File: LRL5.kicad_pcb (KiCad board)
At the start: 2 copper layers, 140 x 50 mm, 31 parts, among them J1 POWER, J2 On/Off, J5 OUT, J6 MODE, Q1 BC549, U1 BA033CC0T, U2 NHD-C0220BIZ

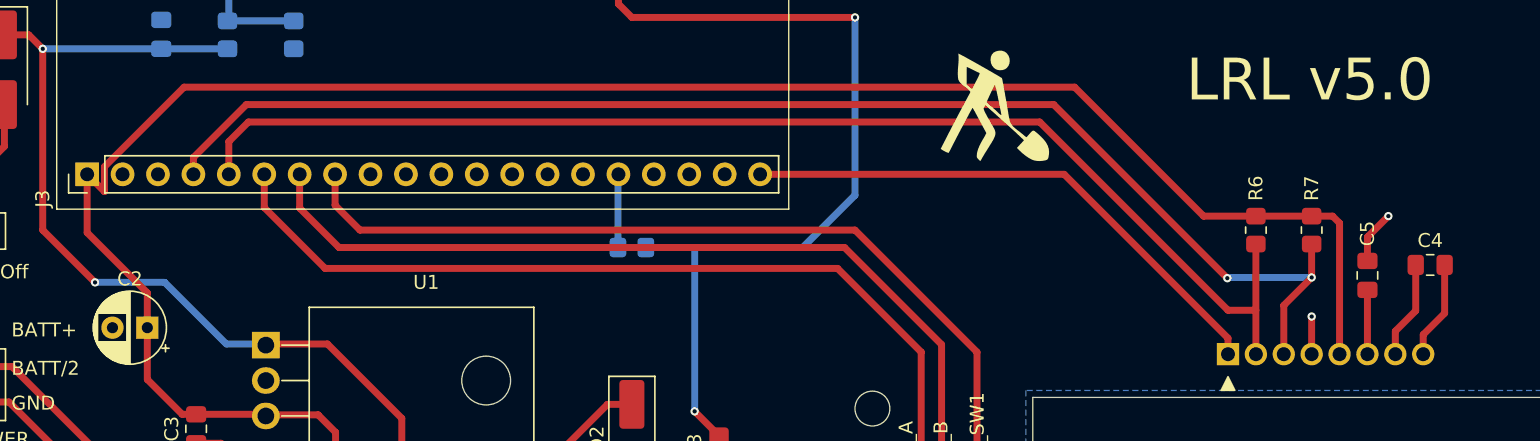
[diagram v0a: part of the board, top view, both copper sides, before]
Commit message: Fix some wires
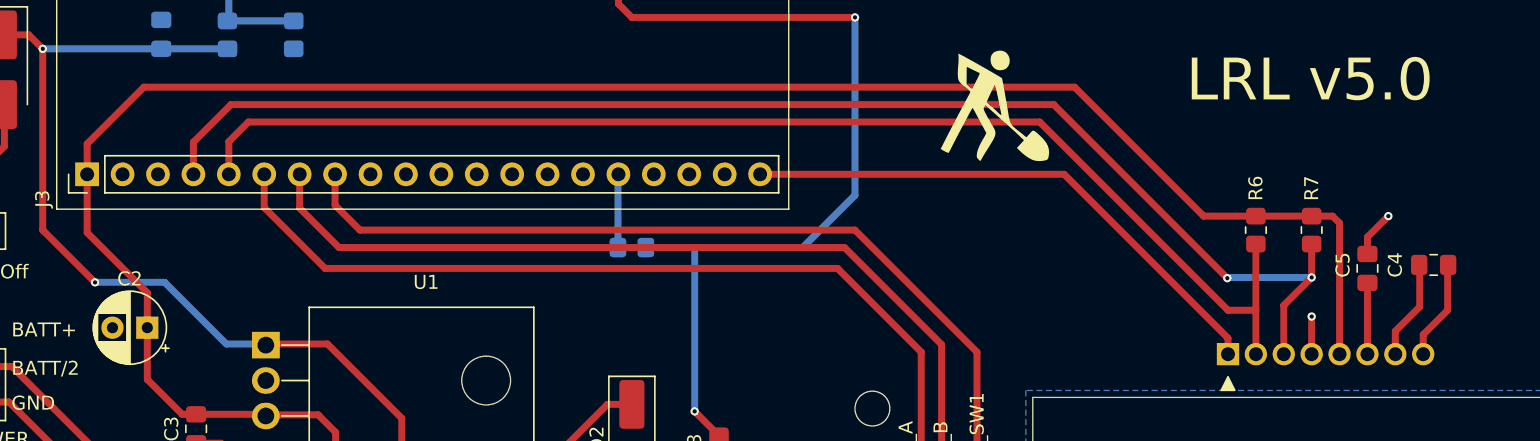
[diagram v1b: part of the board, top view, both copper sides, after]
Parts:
- moved C5 0.50 mm to (229.0, 57.8)
- moved C4 0.25 mm to (233.8, 57.5)
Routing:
- net +3.3V: track 146.8 -> 146.0 mm
- net I2C1_SDA: track 96.9 -> 97.5 mm
- net Net-(U2-VOUT): track 4.61 -> 5.11 mm
- net GND: track 43.4 -> 42.9 mm
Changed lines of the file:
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@@
 	(footprint "Capacitor_SMD:C_0805_2012Metric_Pad1.18x1.45mm_HandSolder"
 		(layer "F.Cu")
-		(at 233.5 57.5)
+		(at 233.75 57.5)
 		(descr "Capacitor SMD 0805 (2012 Metric), square (rectangular) end terminal, IPC_7351 nominal with elongated pad for handsoldering. (Body size source: IPC-SM-782 page 76, https://www.pcb-3d.com/wordpress/wp-content/uploads/ipc-sm-782a_amendment_1_and_2.pdf, https://docs.google.com/spreadsheets/d/1BsfQQcO9C6DZCsRaXUlFlo91Tg2WpOkGARC1WS5S8t0/edit?usp=sharing), generated with kicad-footprint-generator")
 		(tags "capacitor handsolder")
 		(property "Reference" "C4"
-			(at 0 -1.75 0)
+			(at -2.75 0 90)
 			(layer "F.SilkS")
 			(effects
@@
 	(footprint "Capacitor_SMD:C_0805_2012Metric_Pad1.18x1.45mm_HandSolder"
 		(layer "F.Cu")
-		(at 229 58.25 -90)
+		(at 229 57.75 -90)
 		(descr "Capacitor SMD 0805 (2012 Metric), square (rectangular) end terminal, IPC_7351 nominal with elongated pad for handsoldering. (Body size source: IPC-SM-782 page 76, https://www.pcb-3d.com/wordpress/wp-content/uploads/ipc-sm-782a_amendment_1_and_2.pdf, https://docs.google.com/spreadsheets/d/1BsfQQcO9C6DZCsRaXUlFlo91Tg2WpOkGARC1WS5S8t0/edit?usp=sharing), generated with kicad-footprint-generator")
 		(tags "capacitor handsolder")
 		(property "Reference" "C5"
-			(at -3 0 90)
+			(at -0.25 1.75 90)
 			(layer "F.SilkS")
 			(effects
@@
 		)
 		(property "Value" "1uF"
-			(at 0 1.68 90)
+			(at -3.75 0 90)
 			(layer "F.Fab")
 			(effects
@@
 	)
 	(segment
-		(start 230.5 54)
-		(end 229 55.5)
-		(width 0.5)
-		(layer "F.Cu")
-		(net 2)
-	)
-	(segment
 		(start 146.7875 70.2875)
 		(end 149.5 73)
@@
 	)
 	(segment
-		(start 131.58 67.33)
-		(end 138.17 73.92)
+		(start 230.5 54)
+		(end 229 55.5)
 		(width 0.5)
 		(layer "F.Cu")
@@
 	)
 	(segment
-		(start 229 55.5)
-		(end 229 57.2125)
+		(start 131.58 67.33)
+		(end 138.17 73.92)
 		(width 0.5)
 		(layer "F.Cu")
@@
 	)
 	(segment
+		(start 229 55.5)
+		(end 229 56.7125)
+		(width 0.5)
+		(layer "F.Cu")
+		(net 2)
+	)
+	(segment
 		(start 225 63.9)
 		(end 225 61.2)
@@
 	)
 	(segment
-		(start 138.425 50.461522)
-		(end 144.136522 44.75)
-		(width 0.5)
-		(layer "F.Cu")
-		(net 3)
-	)
-	(segment
 		(start 150 68.33)
 		(end 150.08 68.25)
@@
 	)
 	(segment
+		(start 217.25 54)
+		(end 221 54)
+		(width 0.5)
+		(layer "F.Cu")
+		(net 3)
+	)
+	(segment
 		(start 137.185 55.185)
 		(end 141.5 59.5)
@@
 	)
 	(segment
-		(start 149.8825 68.2125)
-		(end 150 68.33)
+		(start 137.185 48.815)
+		(end 141.25 44.75)
 		(width 0.5)
 		(layer "F.Cu")
@@
 	)
 	(segment
-		(start 217.25 54)
-		(end 221 54)
+		(start 149.8825 68.2125)
+		(end 150 68.33)
 		(width 0.5)
 		(layer "F.Cu")
@@
 	)
 	(segment
-		(start 137.185 51)
-		(end 138.425 52.24)
-		(width 0.5)
-		(layer "F.Cu")
-		(net 3)
-	)
-	(segment
 		(start 153.75 68.25)
 		(end 155 69.5)
@@
 	)
 	(segment
-		(start 138.425 52.24)
-		(end 138.425 50.461522)
-		(width 0.5)
-		(layer "F.Cu")
-		(net 3)
-	)
-	(segment
 		(start 227 54.5)
 		(end 226.5 54)
@@
 	)
 	(segment
-		(start 144.136522 44.75)
-		(end 208 44.75)
+		(start 137.185 51)
+		(end 137.185 48.815)
 		(width 0.5)
 		(layer "F.Cu")
@@
 	)
 	(segment
-		(start 233 62.5)
-		(end 233 63.9)
+		(start 141.25 44.75)
+		(end 208 44.75)
+		(width 0.5)
+		(layer "F.Cu")
+		(net 3)
+	)
+	(segment
+		(start 234.75 57.5375)
+		(end 234.75 60.75)
 		(width 0.5)
 		(layer "F.Cu")
@@
 	)
 	(segment
-		(start 234.5375 60.9625)
+		(start 234.75 60.75)
 		(end 233 62.5)
 		(width 0.5)
@@
 	)
 	(segment
-		(start 234.5375 57.5)
-		(end 234.5375 60.9625)
+		(start 233 62.5)
+		(end 233 63.9)
 		(width 0.5)
 		(layer "F.Cu")
@@
 	)
 	(segment
-		(start 232.4625 60.7875)
-		(end 232.4625 57.5)
+		(start 231 63.9)
+		(end 231 62.25)
 		(width 0.5)
 		(layer "F.Cu")
@@
 	)
 	(segment
-		(start 231 62.25)
-		(end 231 63.9)
+		(start 232.75 60.5)
+		(end 232.75 57.5375)
 		(width 0.5)
 		(layer "F.Cu")
@@
 	(segment
 		(start 231 62.25)
-		(end 232.4625 60.7875)
+		(end 232.75 60.5)
 		(width 0.5)
 		(layer "F.Cu")
@@
 	)
 	(segment
-		(start 229 59.2875)
+		(start 229 58.7875)
 		(end 229 63.9)
 		(width 0.5)
@@
 	)
 	(segment
-		(start 218.95 58.45)
-		(end 206.5 46)
+		(start 147.5 46)
+		(end 144.805 48.695)
 		(width 0.5)
 		(layer "F.Cu")
@@
 	)
 	(segment
-		(start 144.805 49.797919)
-		(end 144.805 51)
+		(start 225 58.4)
+		(end 223 60.4)
 		(width 0.5)
 		(layer "F.Cu")
@@
 	)
 	(segment
-		(start 148.602919 46)
-		(end 144.805 49.797919)
+		(start 218.95 58.45)
+		(end 206.5 46)
 		(width 0.5)
 		(layer "F.Cu")
@@
 	)
 	(segment
-		(start 206.5 46)
-		(end 148.602919 46)
+		(start 223 60.4)
+		(end 223 63.9)
 		(width 0.5)
 		(layer "F.Cu")
@@
 	)
 	(segment
-		(start 225 58.4)
-		(end 223 60.4)
+		(start 144.805 48.695)
+		(end 144.805 51)
 		(width 0.5)
 		(layer "F.Cu")
@@
 	)
 	(segment
-		(start 223 60.4)
-		(end 223 63.9)
+		(start 225 58.4)
+		(end 225 56)
 		(width 0.5)
 		(layer "F.Cu")
@@
 	)
 	(segment
-		(start 225 58.4)
-		(end 225 56)
+		(start 206.5 46)
+		(end 147.5 46)
 		(width 0.5)
 		(layer "F.Cu")

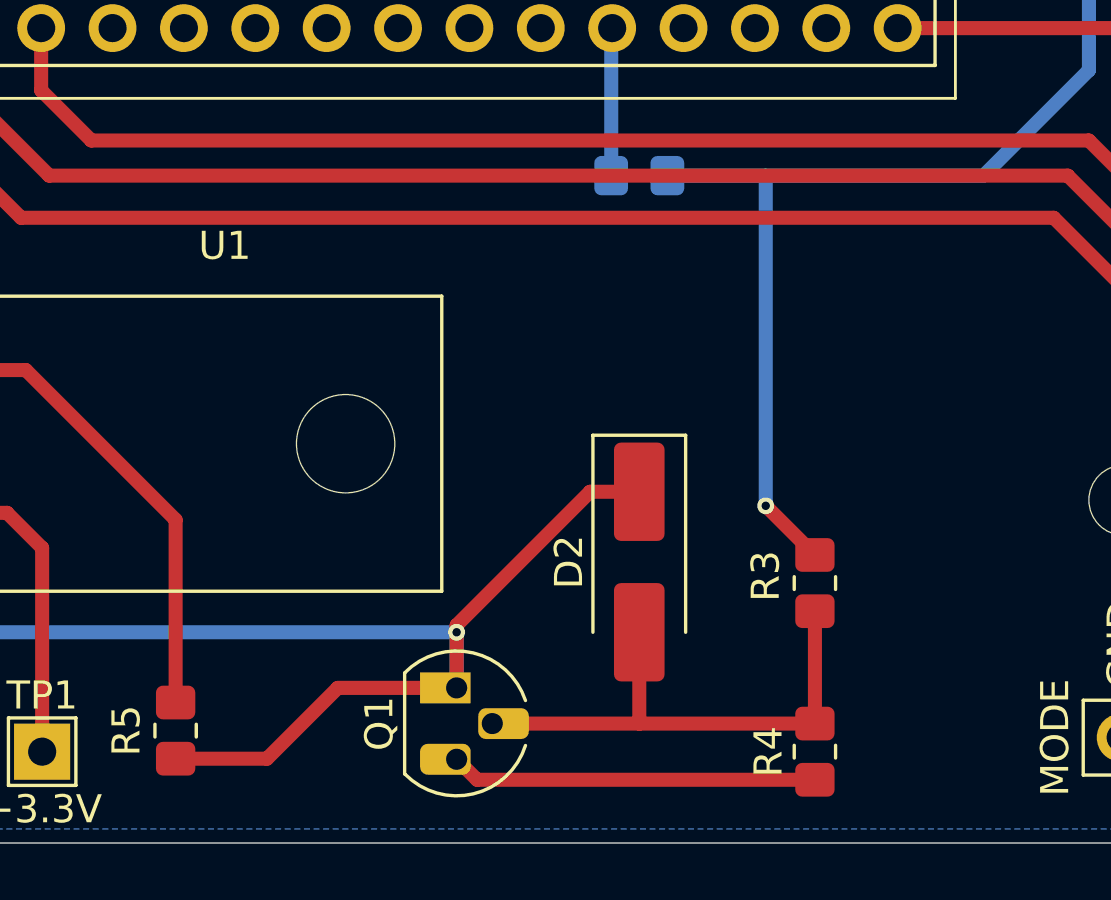
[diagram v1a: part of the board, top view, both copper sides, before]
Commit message: Change BC549 footprint
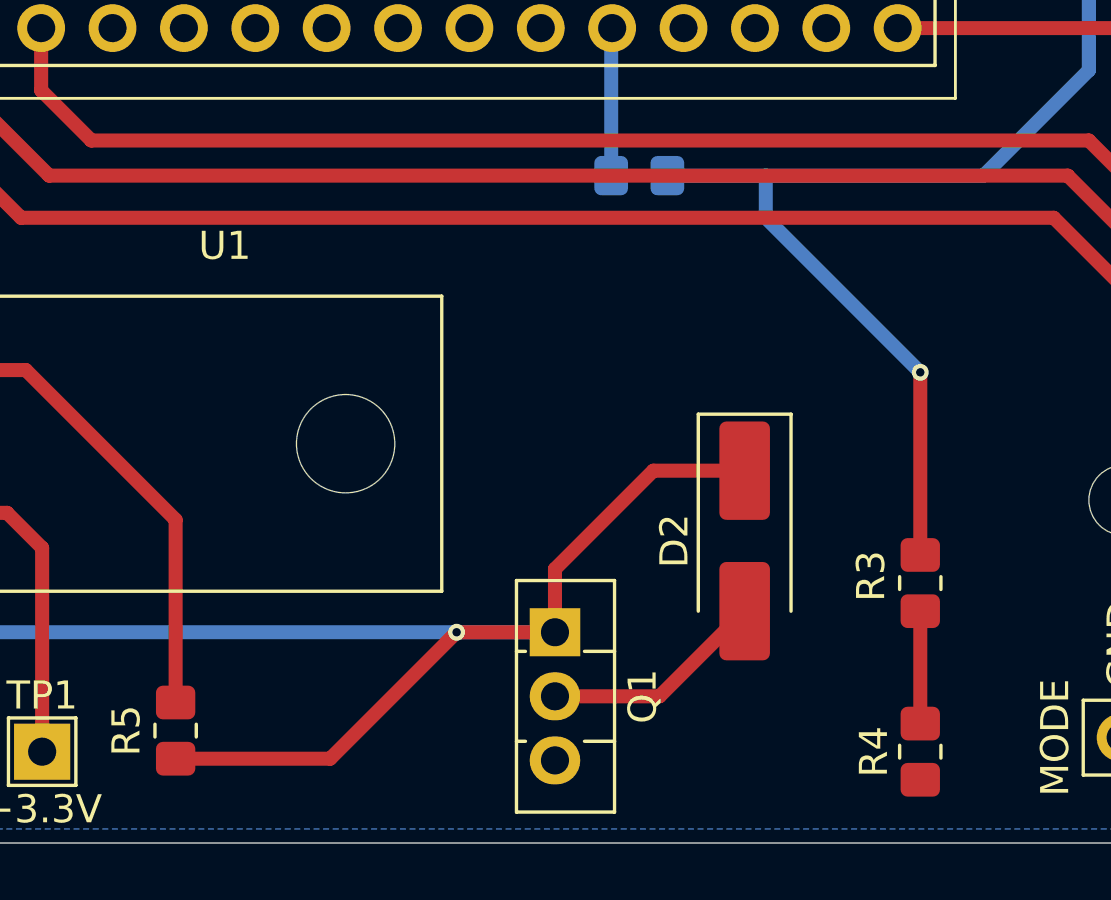
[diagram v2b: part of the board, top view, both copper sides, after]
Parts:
- Q1: footprint Package_TO_SOT_THT:TO-92_HandSolder -> Package_TO_SOT_THT:TO-126-3_Vertical
- moved Q1 4.02 mm to (173.2, 72.5)
- moved D2 3.82 mm to (180.0, 69.2)
- moved R3 3.75 mm to (186.2, 70.8)
- moved R4 3.75 mm to (186.2, 76.8)
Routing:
- net GND: track 42.9 -> 29.9 mm
- net Net-(D2-A): track 18.7 -> 12.0 mm
- net Net-(D2-K): track 53.2 -> 58.8 mm
- net FOUT: track 63.7 -> 65.2 mm

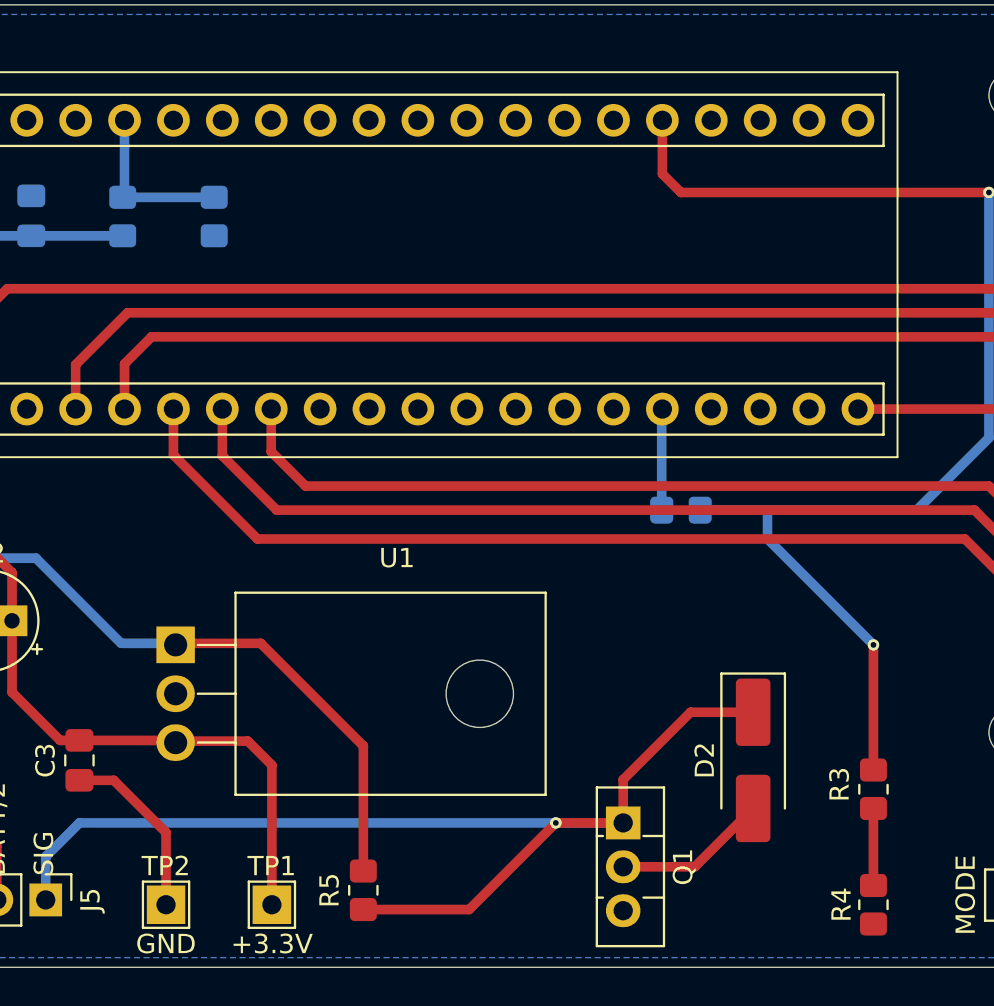
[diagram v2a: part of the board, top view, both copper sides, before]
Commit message: Change some texts
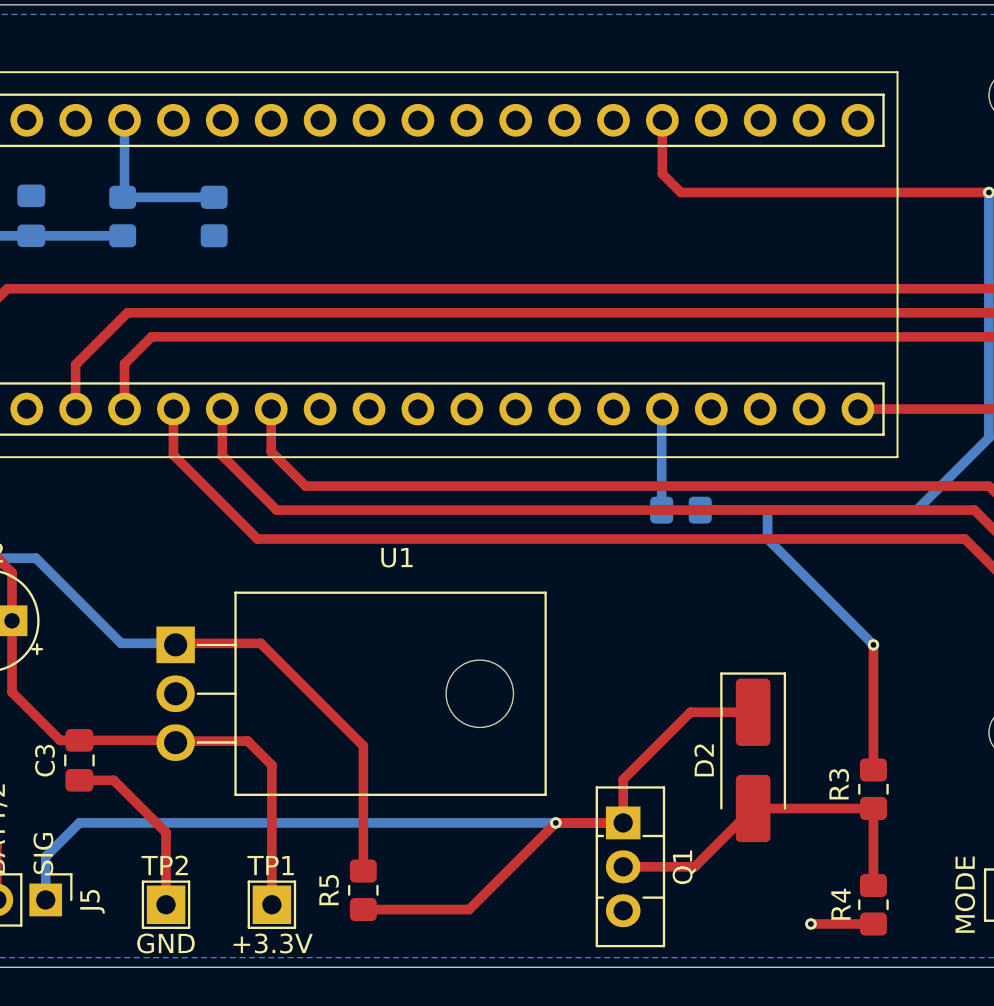
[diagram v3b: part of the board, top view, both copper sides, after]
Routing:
- net Net-(D2-A): track 12.0 -> 18.3 mm
- net GND: track 29.9 -> 33.1 mm, vias 2 -> 3
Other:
- board text added: "B3"
- board text added: "B4"
- board text added: "B5"
- board text added: "B6"
- board text added: "B7"
- board text added: "B8"
- board text added: "B9"
- board text removed: "PB3"
- board text removed: "PB4"
- board text removed: "PB5"
- board text removed: "PB6"
- board text removed: "PB7"
- board text removed: "PB8"
- board text removed: "PB9"
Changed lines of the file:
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@@
 		(layer "Edge.Cuts")
 	)
-	(gr_text "PB3"
+	(gr_text "B3"
 		(at 160.75 52.75 90)
 		(layer "B.SilkS")
@@
 		)
 	)
-	(gr_text "PB8"
-		(at 148 46.2 90)
+	(gr_text "B8"
+		(at 148 47.25 90)
 		(layer "B.SilkS")
 		(effects
@@
 		)
 	)
-	(gr_text "PB4"
+	(gr_text "B4"
 		(at 158 52.75 90)
 		(layer "B.SilkS")
@@
 		)
 	)
-	(gr_text "PB9"
-		(at 145.4 46.2 90)
-		(layer "B.SilkS")
-		(effects
-			(font
-				(size 1 1)
-				(thickness 0.1)
-			)
-			(justify left bottom mirror)
-		)
-	)
-	(gr_text "PB5"
-		(at 155.6 46.2 90)
+	(gr_text "B9"
+		(at 145.4 47.25 90)
+		(layer "B.SilkS")
+		(effects
+			(font
+				(size 1 1)
+				(thickness 0.1)
+			)
+			(justify left bottom mirror)
+		)
+	)
+	(gr_text "B5"
+		(at 155.5 47.25 90)
 		(layer "B.SilkS")
 		(effects
@@
 		)
 	)
-	(gr_text "PB6"
-		(at 153 46.2 90)
+	(gr_text "B6"
+		(at 153 47.25 90)
 		(layer "B.SilkS")
 		(effects
@@
 		)
 	)
-	(gr_text "PB7"
-		(at 150.6 46.2 90)
+	(gr_text "B7"
+		(at 150.6 47.25 90)
 		(layer "B.SilkS")
 		(effects
@@
 	)
 	(segment
+		(start 186.25 77.75)
+		(end 183 77.75)
+		(width 0.5)
+		(layer "F.Cu")
+		(net 2)
+	)
+	(segment
 		(start 229 55.5)
 		(end 229 56.7125)
@@
 		(width 0.5)
 		(layer "F.Cu")
+		(net 2)
+	)
+	(via
+		(at 183 77.75)
+		(size 0.6)
+		(drill 0.3)
+		(layers "F.Cu" "B.Cu")
 		(net 2)
 	)
@@
 	)
 	(segment
+		(start 186.25 71.75)
+		(end 180 71.75)
+		(width 0.5)
+		(layer "F.Cu")
+		(net 9)
+	)
+	(segment
 		(start 173.25 74.78)
 		(end 176.97 74.78)
@@
 	)
 	(segment
-		(start 147.125 36.22)
-		(end 147.345 36)
-		(width 0.5)
-		(layer "B.Cu")
-		(net 31)
-	)
-	(segment

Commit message: Added filled zone
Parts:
- J3, J4: footprint Connector_PinHeader_2.54mm:PinHeader_1x20_P2.54mm_Vertical -> Connector_PinHeader_2.54mm:PinHeader_1x20_P2.54mm_Vertical_SMD_Pin1Left
- R8: moved to F.Cu
- moved G*** 47.2 mm to (249.0, 42.2)
- moved R8 27.4 mm to (149.0, 58.6)
- moved J3 23.9 mm to (161.1, 51.1), turned to -90 degrees
- moved J4 23.9 mm to (161.1, 36.1), turned to -90 degrees
- moved J6 7.50 mm to (193.5, 76.5), turned to 90 degrees
- moved D2 4.93 mm to (175.8, 66.8), turned to 0 degrees
- moved C1 4.00 mm to (138.5, 41.0)
- moved R1 4.00 mm to (143.2, 41.0)
- moved R2 4.00 mm to (148.0, 41.0)
- moved R3 3.25 mm to (183.0, 70.8)
- moved R4 3.25 mm to (183.0, 76.8)
- moved TP1 1.95 mm to (155.0, 74.8)
- moved TP2 1.95 mm to (149.5, 74.8)
- moved R5 0.65 mm to (160.4, 76.0)
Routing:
- net LCD_RESET: track 39.6 -> 100.8 mm
- net I2C1_SDA: track 97.5 -> 60.2 mm
- net VBAT: track 8.83 -> 37.3 mm, vias 0 -> 1
- net I2C1_SCL: track 90.2 -> 62.1 mm, vias 0 -> 2
- net MODE_A: track 65.1 -> 38.5 mm
- net MODE_B: track 65.6 -> 41.5 mm
- net MODE_SW1: track 66.7 -> 43.3 mm
- net +3.3V: track 146.0 -> 127.6 mm, vias 0 -> 4
- net Net-(D2-K): track 58.8 -> 42.5 mm
- net +BATT: track 67.3 -> 63.6 mm
- net GND: track 33.1 -> 34.9 mm, vias 3 -> 4
- net Net-(D2-A): track 18.3 -> 20.0 mm
- net FOUT: track 65.2 -> 63.5 mm
- net FIN: track 5.26 -> 6.23 mm
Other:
- board text added: "+3.3"
- board text added: "LRL v5.1"
- board text removed: "+3.3V"
- board text removed: "A0"
- board text removed: "A8"
- board text removed: "B11"
- board text removed: "B12"
- board text removed: "B5"
- board text removed: "B6"
- board text removed: "B7"
- board text removed: "B8"
- board text removed: "B9"
- board text removed: "LRL v5.0"
- board text removed: "USART1_RX"
- board text removed: "USART1_TX"

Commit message: Some fixes
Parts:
- C1, R1, R2: moved to F.Cu
- G***: moved to B.Cu
- H1, H2, H3, H4: footprint MountingHole:MountingHole_2.5mm -> MountingHole:MountingHole_3.2mm_M3
- J2: footprint Connector_PinHeader_2.54mm:PinHeader_1x02_P2.54mm_Vertical -> Connector_PinHeader_2.54mm:PinHeader_1x02_P2.54mm_Vertical_SMD_Pin1Left
- J5: footprint Connector_PinHeader_2.54mm:PinHeader_1x03_P2.54mm_Vertical -> Connector_PinHeader_2.54mm:PinHeader_1x03_P2.54mm_Vertical_SMD_Pin1Left
- J6: footprint Connector_PinHeader_2.54mm:PinHeader_1x04_P2.54mm_Vertical -> Connector_PinHeader_2.54mm:PinHeader_1x04_P2.54mm_Vertical_SMD_Pin1Left
- moved J2 133.0 mm to (262.8, 60.2)
- moved D1 108.8 mm to (237.6, 66.3), turned to 90 degrees
- moved J5 108.5 mm to (251.8, 74.2), turned to 0 degrees
- moved J1 108.1 mm to (237.0, 77.3), turned to 90 degrees
- moved C1 72.2 mm to (205.5, 68.0), turned to 180 degrees
- moved R1 66.2 mm to (205.5, 63.5), turned to 180 degrees
- moved J3 65.8 mm to (226.9, 51.3)
- moved J4 65.8 mm to (226.9, 36.3)
- moved U1 61.7 mm to (211.2, 70.9)
- moved C3 59.8 mm to (204.5, 75.0), turned to 90 degrees
- moved C2 59.4 mm to (199.2, 76.0), turned to 90 degrees
- moved R2 56.8 mm to (199.8, 64.5)
- moved R8 50.2 mm to (196.8, 43.0), turned to -90 degrees
- moved H1 43.8 mm to (174.8, 33.5)
- moved H3 43.8 mm to (174.8, 76.5)
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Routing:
- net LCD_RESET: track 100.8 -> 19.3 mm
- net Net-(D2-K): track 42.5 -> 94.4 mm, vias 1 -> 2
- net FOUT: track 63.5 -> 24.0 mm, vias 2 -> 0
- net MODE_SW1: track 43.3 -> 77.1 mm, vias 0 -> 2
- net MODE_A: track 38.5 -> 71.9 mm, vias 0 -> 2
- net MODE_B: track 41.5 -> 74.8 mm, vias 0 -> 2
- net Net-(J1-Pin_1): track 7.21 -> 34.8 mm
- net I2C1_SDA: track 60.2 -> 32.8 mm, vias 2 -> 1
- net +3.3V: track 127.6 -> 100.3 mm, vias 4 -> 3
- net I2C1_SCL: track 62.1 -> 39.9 mm, vias 2 -> 1
- net VBAT: track 37.3 -> 58.9 mm, vias 1 -> 2
- net Net-(D1-A): track 7.02 -> 25.5 mm
- net FIN: track 6.23 -> 22.8 mm
- net +BATT: track 63.6 -> 53.4 mm, vias 2 -> 0
- net GND: track 34.9 -> 44.1 mm, vias 4 -> 5
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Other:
- board size 140 x 50 mm -> 96.2 x 50 mm
